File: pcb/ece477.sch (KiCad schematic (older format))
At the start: 9 parts, among them J1 Micro_SD_Card, SW1 SW_Push, U1 ESP32-WROOM-32, U2 ADA751

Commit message: updated pcb
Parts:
- removed J1: Micro_SD_Card, Connector_Card:microSD_HC_Hirose_DM3BT-DSF-PEJS, symbol Connector:Micro_SD_Card
- removed U2: ADA751, symbol Device:ADA751
- added J1: ADA751, Connector_PinHeader_2.00mm:PinHeader_1x05_P2.00mm_Vertical, symbol Connector_Generic:Conn_01x05
- added J2: ADA254, Connector_PinHeader_2.00mm:PinHeader_1x08_P2.00mm_Vertical, symbol Connector:Conn_01x08_Male
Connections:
- wire segments 49 -> 47
- no-connect marks 0 -> 3
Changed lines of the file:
@@
 pcb/ece477.sch
-$Comp
-L Device:ADA751 U2
-U 1 1 5F6473B1
-P 6850 4850
-F 0 "U2" H 7228 5276 50  0000 L CNN
-F 1 "ADA751" H 7228 5185 50  0000 L CNN
-F 2 "" H 6850 4850 50  0001 C CNN
-F 3 "" H 6850 4850 50  0001 C CNN
-	1    6850 4850
-	1    0    0    -1
-$EndComp
 $Comp
 L RF_Module:ESP32-WROOM-32 U1
@@
 F 3 "https://www.espressif.com/sites/default/files/documentation/esp32-wroom-32_datasheet_en.pdf" H 4000 3900 50  0001 C CNN
 	1    4300 3850
-	1    0    0    -1
-$EndComp
-$Comp
-L Connector:Micro_SD_Card J1
-U 1 1 5F55F02A
-P 7400 3350
-F 0 "J1" H 7350 4067 50  0000 C CNN
-F 1 "Micro_SD_Card" H 7350 3976 50  0000 C CNN
-F 2 "Connector_Card:microSD_HC_Hirose_DM3BT-DSF-PEJS" H 8550 3650 50  0001 C CNN
-F 3 "http://katalog.we-online.de/em/datasheet/693072010801.pdf" H 7400 3350 50  0001 C CNN
-	1    7400 3350
 	1    0    0    -1
 $EndComp
@@
 $EndComp
 Wire Wire Line
-	6400 4300 5900 4300
-Wire Wire Line
 	5900 4300 5900 3650
 Wire Wire Line
 	5900 3650 4900 3650
 Wire Wire Line
-	6400 4450 5500 4450
-Wire Wire Line
-	5500 4450 5500 3750
-Wire Wire Line
 	5500 3750 4900 3750
 Wire Wire Line
-	6400 4600 6150 4600
-Wire Wire Line
-	6150 4600 6150 5350
-Wire Wire Line
 	5250 3550 6000 3550
 Wire Wire Line
-	6000 3550 6000 4150
-Wire Wire Line
-	6000 4150 6400 4150
-Wire Wire Line
 	5250 1700 5300 1700
 Wire Wire Line
 	5600 1700 5700 1700
-Wire Wire Line
-	6500 3650 6100 3650
-Wire Wire Line
-	6100 3650 6100 3250
-Wire Wire Line
-	6100 3250 4900 3250
-Wire Wire Line
-	6500 3250 6150 3250
-Wire Wire Line
-	6150 3350 5600 3350
-Wire Wire Line
-	6150 3250 6150 3350
-Wire Wire Line
-	6500 3350 6350 3350
-Wire Wire Line
-	6350 3350 6350 2500
-Wire Wire Line
-	6350 2500 5700 2500
 Wire Wire Line
 	5700 2500 5700 1700
@@
 	5700 1700 5750 1700
 Wire Wire Line
-	6500 3450 4900 3450
-Wire Wire Line
-	6500 3150 5100 3150
-Wire Wire Line
-	5100 3150 5100 3550
-Wire Wire Line
-	5100 3550 4900 3550
-Wire Wire Line
-	6500 3550 6150 3550
-Wire Wire Line
-	6150 3550 6150 4600
-Connection ~ 6150 4600
-Wire Wire Line
 	5100 5350 6150 5350
 Wire Wire Line
-	5600 2950 5600 3350
-Connection ~ 5600 3350
-Wire Wire Line
-	5600 3350 4900 3350
-Wire Wire Line
 	5600 2650 5600 2500
 Wire Wire Line
 	5600 2500 5700 2500
-Connection ~ 5700 2500
 $Comp
 L Device:C C1
@@
 Wire Wire Line
 	4450 1300 6300 1300
+$Comp
+L Connector:Conn_01x08_Male J2
+U 1 1 5F66F62E
+P 6700 3350
+F 0 "J2" H 6672 3232 50  0000 R CNN
+F 1 "ADA254" H 6672 3323 50  0000 R CNN
+F 2 "Connector_PinHeader_2.00mm:PinHeader_1x08_P2.00mm_Vertical" H 6700 3350 50  0001 C CNN
+F 3 "~" H 6700 3350 50  0001 C CNN
+	1    6700 3350
+	-1   0    0    1
+$EndComp
+Wire Wire Line
+	4900 3250 6500 3250
+Wire Wire Line
+	4900 3350 5600 3350
+Wire Wire Line
+	5600 3350 5600 3150
+Wire Wire Line
+	5600 3150 6500 3150
+Wire Wire Line
+	4900 3450 5950 3450
+Wire Wire Line
+	5950 3450 5950 3350
+Wire Wire Line
+	5950 3350 6500 3350
+Wire Wire Line
+	4900 3550 5150 3550
+Wire Wire Line
+	5150 3550 5150 3050
+Wire Wire Line
+	5150 3050 6500 3050
+Wire Wire Line
+	6500 3450 6150 3450
+Wire Wire Line
+	5600 2950 5600 3150
+Connection ~ 5600 3150
+Wire Wire Line
+	6000 3550 6500 3550
+Connection ~ 6000 3550
+Wire Wire Line
+	6150 3450 6150 4500
+$Comp
+L Connector_Generic:Conn_01x05 J1
+U 1 1 5F679D6C
+P 6650 4400
+F 0 "J1" H 6730 4442 50  0000 L CNN
+F 1 "ADA751" H 6730 4351 50  0000 L CNN
+F 2 "Connector_PinHeader_2.00mm:PinHeader_1x05_P2.00mm_Vertical" H 6650 4400 50  0001 C CNN
+F 3 "~" H 6650 4400 50  0001 C CNN
+	1    6650 4400
+	1    0    0    -1
+$EndComp
+Wire Wire Line
+	6000 4200 6450 4200
+Wire Wire Line
+	6000 3550 6000 4200
+Wire Wire Line
+	5900 4300 6450 4300
+Wire Wire Line
+	5500 3750 5500 4400
+Wire Wire Line
+	5500 4400 6450 4400
+Wire Wire Line
+	6450 4500 6150 4500
+Connection ~ 6150 4500
+Wire Wire Line
+	6150 4500 6150 5350
+NoConn ~ 6450 4600
+NoConn ~ 6500 2950
+NoConn ~ 6500 3650
+Wire Wire Line
+	4850 2050 4850 1700
+Connection ~ 4850 1700
 $EndSCHEMATC

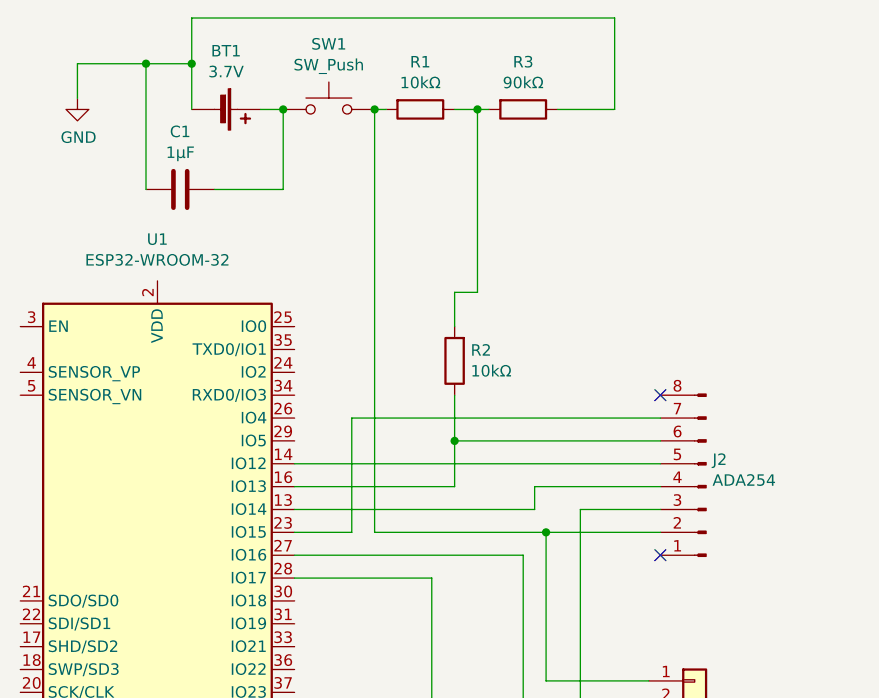
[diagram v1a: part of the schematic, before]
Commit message: added wires to pcb
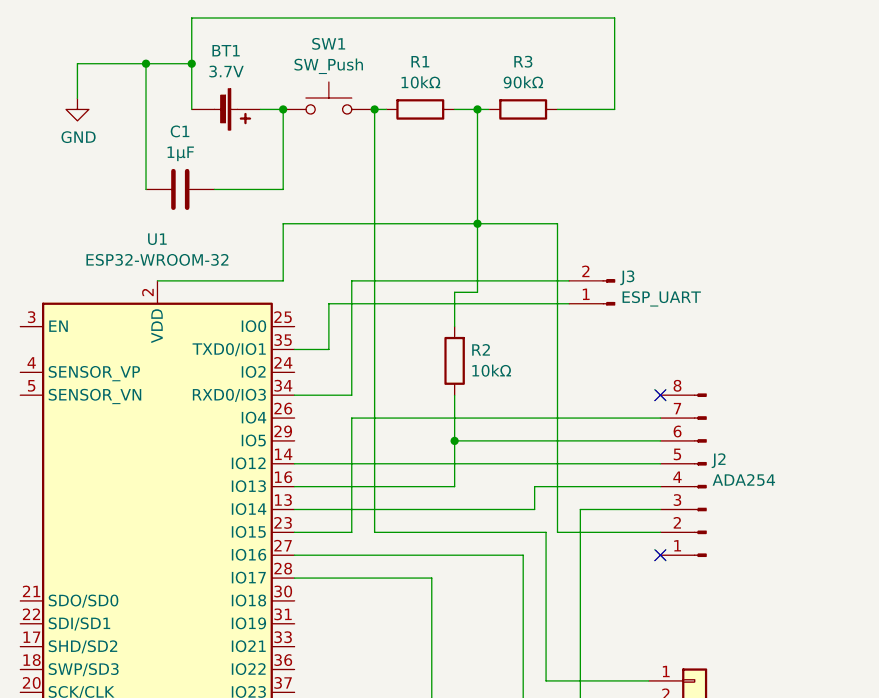
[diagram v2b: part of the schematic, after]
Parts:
- added J3: ESP_UART, Connector_PinHeader_2.00mm:PinHeader_1x02_P2.00mm_Vertical, symbol Connector:Conn_01x02_Male
- BT1: footprint Battery:Battery_Panasonic_CR1025-VSK_Vertical_CircularHoles -> Connector_PinHeader_2.00mm:PinHeader_1x02_P2.00mm_Vertical
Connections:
- net at U1.2 (VDD): now also J2.2 (Pin_2), R1.1, R2.2, R3.2
- net at U1.34 (RXD0/IO3): now also J3.2 (Pin_2)
- net at U1.35 (TXD0/IO1): now also J3.1 (Pin_1)
- net at J1.1 (Pin_1), R1.2, SW1.2: no longer J2.2 (Pin_2)
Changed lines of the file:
@@
 F 0 "BT1" V 4295 1750 50  0000 C CNN
 F 1 "3.7V" V 4386 1750 50  0000 C CNN
-F 2 "Battery:Battery_Panasonic_CR1025-VSK_Vertical_CircularHoles" V 4550 1760 50  0001 C CNN
+F 2 "Connector_PinHeader_2.00mm:PinHeader_1x02_P2.00mm_Vertical" V 4550 1760 50  0001 C CNN
 F 3 "~" V 4550 1760 50  0001 C CNN
 	1    4550 1700
@@
 	5500 3750 4900 3750
 Wire Wire Line
-	5250 3550 6000 3550
-Wire Wire Line
 	5250 1700 5300 1700
 Wire Wire Line
 	5600 1700 5700 1700
 Wire Wire Line
-	5700 2500 5700 1700
+	5700 2500 5700 2200
 Connection ~ 5700 1700
 Wire Wire Line
@@
 Connection ~ 5600 3150
 Wire Wire Line
-	6000 3550 6500 3550
-Connection ~ 6000 3550
-Wire Wire Line
 	6150 3450 6150 4500
 $Comp
@@
 	6000 4200 6450 4200
 Wire Wire Line
-	6000 3550 6000 4200
-Wire Wire Line
 	5900 4300 6450 4300
 Wire Wire Line
@@
 	4850 2050 4850 1700
 Connection ~ 4850 1700
+$Comp
+L Connector:Conn_01x02_Male J3
+U 1 1 5F664963
+P 6300 2550
+F 0 "J3" H 6272 2432 50  0000 R CNN
+F 1 "ESP_UART" H 6272 2523 50  0000 R CNN
+F 2 "Connector_PinHeader_2.00mm:PinHeader_1x02_P2.00mm_Vertical" H 6300 2550 50  0001 C CNN
+F 3 "~" H 6300 2550 50  0001 C CNN
+	1    6300 2550
+	-1   0    0    1
+$EndComp
+Wire Wire Line
+	5150 2450 6100 2450
+Wire Wire Line
+	4300 2450 4850 2450
+Wire Wire Line
+	4850 2450 4850 2200
+Connection ~ 5700 2200
+Wire Wire Line
+	5700 2200 5700 1700
+Wire Wire Line
+	5250 3550 6000 3550
+Wire Wire Line
+	6000 3550 6000 4200
+Wire Wire Line
+	4850 2200 5700 2200
+Wire Wire Line
+	5700 2200 6050 2200
+Wire Wire Line
+	6050 2200 6050 3550
+Wire Wire Line
+	6050 3550 6500 3550
+Wire Wire Line
+	4900 2950 5150 2950
+Wire Wire Line
+	5150 2450 5150 2950
+Wire Wire Line
+	5050 2550 5050 2750
+Wire Wire Line
+	5050 2750 4900 2750
+Wire Wire Line
+	5050 2550 6100 2550
 $EndSCHEMATC

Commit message: cleanup
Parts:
- removed J1: ADA751, Connector_PinHeader_2.00mm:PinHeader_1x05_P2.00mm_Vertical, symbol Connector_Generic:Conn_01x05
- removed J2: ADA254, Connector_PinHeader_2.00mm:PinHeader_1x08_P2.00mm_Vertical, symbol Connector:Conn_01x08_Male
- removed J3: ESP_UART, Connector_PinHeader_2.00mm:PinHeader_1x02_P2.00mm_Vertical, symbol Connector:Conn_01x02_Male
- removed R2: 10kΩ, Resistor_SMD:R_0201_0603Metric, symbol Device:R
- removed R3: 90kΩ, Resistor_SMD:R_0201_0603Metric, symbol Device:R
- removed SW1: SW_Push, Button_Switch_SMD:SW_DIP_SPSTx01_Slide_6.7x4.1mm_W6.73mm_P2.54mm_LowProfile_JPin, symbol Switch:SW_Push
- added C2: 10µF, Capacitor_SMD:CP_Elec_3x5.3, symbol Device:C
- added C3: 4.7µF, Capacitor_SMD:CP_Elec_3x5.3, symbol Device:C
- added C4: 100nF, Capacitor_SMD:CP_Elec_3x5.3, symbol Device:C
- added C5: 10nF, Capacitor_SMD:CP_Elec_3x5.3, symbol Device:C
- added FB1: Ferrite_Bead, Ferrite_THT:LairdTech_28C0236-0JW-10, symbol Device:Ferrite_Bead
- added J1: USB_A, digikey-footprints:USB_Male_A_UP2-AH-1-TH, symbol Connector:USB_A
- added L1: 2.2µH, Inductor_SMD:L_7.3x7.3_H4.5, symbol Device:L
- added SW1: SW_DIP_x01, Button_Switch_SMD:SW_DIP_SPSTx01_Slide_6.7x4.1mm_W6.73mm_P2.54mm_LowProfile_JPin, symbol Switch:SW_DIP_x01
- added U2: FT232RL-REEL, digikey-footprints:SSOP-28_W5.30mm, symbol dk_Interface-Controllers:FT232RL-REEL
- added U3: LM3671, Package_TO_SOT_SMD:TSOT-23-5, symbol Regulator_Switching:LM3670MF
- added U4: ADA254, Connector_PinSocket_2.00mm:PinSocket_1x08_P2.00mm_Vertical, symbol Device:ADA254
- added U5: ADA751, Connector_PinHeader_2.00mm:PinHeader_1x05_P2.00mm_Vertical, symbol Device:ADA751
- BT1: footprint Connector_PinHeader_2.00mm:PinHeader_1x02_P2.00mm_Vertical -> Button_Switch_SMD:SW_DIP_SPSTx01_Slide_6.7x4.1mm_W6.73mm_P2.54mm_LowProfile_JPin
- C1: value 1µF -> 4.7µF
- U1: footprint Package_DFN_QFN:QFN-48-1EP_5x5mm_P0.35mm_EP3.7x3.7mm -> digikey-footprints:ESP32-WROOM-32D
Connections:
- net GND: now also C2.1, C3.1, C4.1, C5.2, J1.4 (GND), U2.18 (GND), U2.21 (GND), U2.25 (AGND), U2.26 (TEST), U2.7 (GND), U3.2 (GND), U4.6 (GND), U5.4 (GND); no longer U1.1 (GND), U1.15 (GND), U1.38 (GND), U1.39 (GND)
- net at U1.13 (IO14): now also U4.5 (CLK)
- net at U1.14 (IO12): now also U4.4 (DO)
- net at U1.16 (IO13): now also R1.2, U4.3 (DI)
- net at R1.1, U1.2 (VDD): now also C2.2, FB1.2, L1.1, U2.20 (VCC), U2.4 (VCCIO), U3.4 (FB), U4.7 (3V)
- net at U1.23 (IO15): now also U4.2 (CS)
- net at U1.27 (IO16): now also U5.2 (TD)
- net at U1.28 (IO17): now also U5.3 (RD)
- net at U1.34 (RXD0/IO3): now also U2.1 (TXD)
- net at U1.35 (TXD0/IO1): now also U2.5 (RXD)
- net at BT1.1 (+), C1.2: now also SW1.1
- new net: U1.1 (GND), U1.15 (GND), U1.38 (GND), U1.39 (GND)
- new net: C3.2, SW1.2, U3.1 (Vin), U3.3 (EN), U5.1 (Vin)
- new net: C4.2, U2.17 (3V3OUT)
- new net: C5.1, FB1.1, J1.1 (VBUS)
- new net: J1.2 (D-), U2.16 (USBDM)
- new net: J1.3 (D+), U2.15 (USBDP)
- new net: L1.2, U3.5 (SW)
- no-connect marks 3 -> 2
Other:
- note added: "Oct 1, 2020"
- note removed: "Sep 6, 2020"
- note removed: "pcb/ece477.sch"
- moved on the sheet: BT1, C1, U1

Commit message: uploaded pcb files
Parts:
- BT1: footprint Button_Switch_SMD:SW_DIP_SPSTx01_Slide_6.7x4.1mm_W6.73mm_P2.54mm_LowProfile_JPin -> Connector_PinHeader_2.00mm:PinHeader_1x02_P2.00mm_Vertical
- C1, C2, C3, C4, C5: footprint Capacitor_SMD:CP_Elec_3x5.3 -> Capacitor_SMD:C_0201_0603Metric
- J1: footprint digikey-footprints:USB_Male_A_UP2-AH-1-TH -> digikey-footprints:USB_Mini_B_Female_690-005-299-043
- L1: footprint Inductor_SMD:L_7.3x7.3_H4.5 -> Inductor_SMD:L_0201_0603Metric
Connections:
- net GND: now also U1.1 (GND), U1.15 (GND), U1.38 (GND), U1.39 (GND)
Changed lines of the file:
@@
 F 0 "C1" V 4002 2300 50  0000 C CNN
 F 1 "4.7µF" V 3911 2300 50  0000 C CNN
-F 2 "Capacitor_SMD:CP_Elec_3x5.3" H 3788 2150 50  0001 C CNN
+F 2 "Capacitor_SMD:C_0201_0603Metric" H 3788 2150 50  0001 C CNN
 F 3 "~" H 3750 2300 50  0001 C CNN
 	1    3750 2300
@@
 F 0 "BT1" V 3645 2000 50  0000 C CNN
 F 1 "3.7V" V 3736 2000 50  0000 C CNN
-F 2 "Button_Switch_SMD:SW_DIP_SPSTx01_Slide_6.7x4.1mm_W6.73mm_P2.54mm_LowProfile_JPin" V 3900 2010 50  0001 C CNN
+F 2 "Connector_PinHeader_2.00mm:PinHeader_1x02_P2.00mm_Vertical" V 3900 2010 50  0001 C CNN
 F 3 "~" V 3900 2010 50  0001 C CNN
 	1    3900 1950
@@
 F 0 "C2" V 5652 1700 50  0000 C CNN
 F 1 "10µF" V 5561 1700 50  0000 C CNN
-F 2 "Capacitor_SMD:CP_Elec_3x5.3" H 5438 1550 50  0001 C CNN
+F 2 "Capacitor_SMD:C_0201_0603Metric" H 5438 1550 50  0001 C CNN
 F 3 "~" H 5400 1700 50  0001 C CNN
 	1    5400 1700
@@
 F 0 "L1" H 5452 2046 50  0000 L CNN
 F 1 "2.2µH" H 5452 1955 50  0000 L CNN
-F 2 "Inductor_SMD:L_7.3x7.3_H4.5" H 5400 2000 50  0001 C CNN
+F 2 "Inductor_SMD:L_0201_0603Metric" H 5400 2000 50  0001 C CNN
 F 3 "~" H 5400 2000 50  0001 C CNN
 	1    5400 2000
@@
 	-1   0    0    1
 $EndComp
-Wire Wire Line
-	3600 1550 5400 1550
 Connection ~ 5400 1550
 Wire Wire Line
@@
 F 0 "C3" V 6602 1700 50  0000 C CNN
 F 1 "4.7µF" V 6511 1700 50  0000 C CNN
-F 2 "Capacitor_SMD:CP_Elec_3x5.3" H 6388 1550 50  0001 C CNN
+F 2 "Capacitor_SMD:C_0201_0603Metric" H 6388 1550 50  0001 C CNN
 F 3 "~" H 6350 1700 50  0001 C CNN
 	1    6350 1700
@@
 F 0 "C4" H 7215 3046 50  0000 L CNN
 F 1 "100nF" H 7215 2955 50  0000 L CNN
-F 2 "Capacitor_SMD:CP_Elec_3x5.3" H 7138 2850 50  0001 C CNN
+F 2 "Capacitor_SMD:C_0201_0603Metric" H 7138 2850 50  0001 C CNN
 F 3 "~" H 7100 3000 50  0001 C CNN
 	1    7100 3000
@@
 F 0 "J1" H 8770 1847 50  0000 R CNN
 F 1 "USB_A" H 8770 1938 50  0000 R CNN
-F 2 "digikey-footprints:USB_Male_A_UP2-AH-1-TH" H 9150 1900 50  0001 C CNN
+F 2 "digikey-footprints:USB_Mini_B_Female_690-005-299-043" H 9150 1900 50  0001 C CNN
 F 3 " ~" H 9150 1900 50  0001 C CNN
 	1    9000 1950
@@
 F 0 "C5" H 9115 1446 50  0000 L CNN
 F 1 "10nF" H 9115 1355 50  0000 L CNN
-F 2 "Capacitor_SMD:CP_Elec_3x5.3" H 9038 1250 50  0001 C CNN
+F 2 "Capacitor_SMD:C_0201_0603Metric" H 9038 1250 50  0001 C CNN
 F 3 "~" H 9000 1400 50  0001 C CNN
 	1    9000 1400
@@
 Connection ~ 7400 1550
 Connection ~ 7500 1550
+Wire Wire Line
+	3600 1550 5400 1550
+Wire Wire Line
+	6050 6050 4850 6050
+Wire Wire Line
+	4850 6050 4850 6100
+Wire Wire Line
+	4850 6100 4650 6100
 $EndSCHEMATC

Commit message: pcb update
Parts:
- J1: value USB_A -> USB_B; footprint digikey-footprints:USB_Mini_B_Female_690-005-299-043 -> Connector_USB:USB_Micro-B_Molex_47346-0001
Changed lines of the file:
@@
 P 9000 1950
 F 0 "J1" H 8770 1847 50  0000 R CNN
-F 1 "USB_A" H 8770 1938 50  0000 R CNN
-F 2 "digikey-footprints:USB_Mini_B_Female_690-005-299-043" H 9150 1900 50  0001 C CNN
+F 1 "USB_B" H 8770 1938 50  0000 R CNN
+F 2 "Connector_USB:USB_Micro-B_Molex_47346-0001" H 9150 1900 50  0001 C CNN
 F 3 " ~" H 9150 1900 50  0001 C CNN
 	1    9000 1950
